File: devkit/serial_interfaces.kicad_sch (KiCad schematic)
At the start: 15 parts, among them J1 Micro_SD_Card, J2 Conn_01x03, J3 Conn_01x04, J4 Conn_01x06, U4 BME280, U5 BH1750, U6 MPU6050

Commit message: chore: actualizo algunas huellas e info en pcb
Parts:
- C6: footprint Capacitor_SMD:CP_Elec_4x5.8 -> Capacitor_SMD:C_0805_2012Metric_Pad1.18x1.45mm_HandSolder
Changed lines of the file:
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@@
 			)
 		)
-		(property "Footprint" "Capacitor_SMD:CP_Elec_4x5.8"
+		(property "Footprint" "Capacitor_SMD:C_0805_2012Metric_Pad1.18x1.45mm_HandSolder"
 			(at 44.1452 140.97 0)
 			(effects

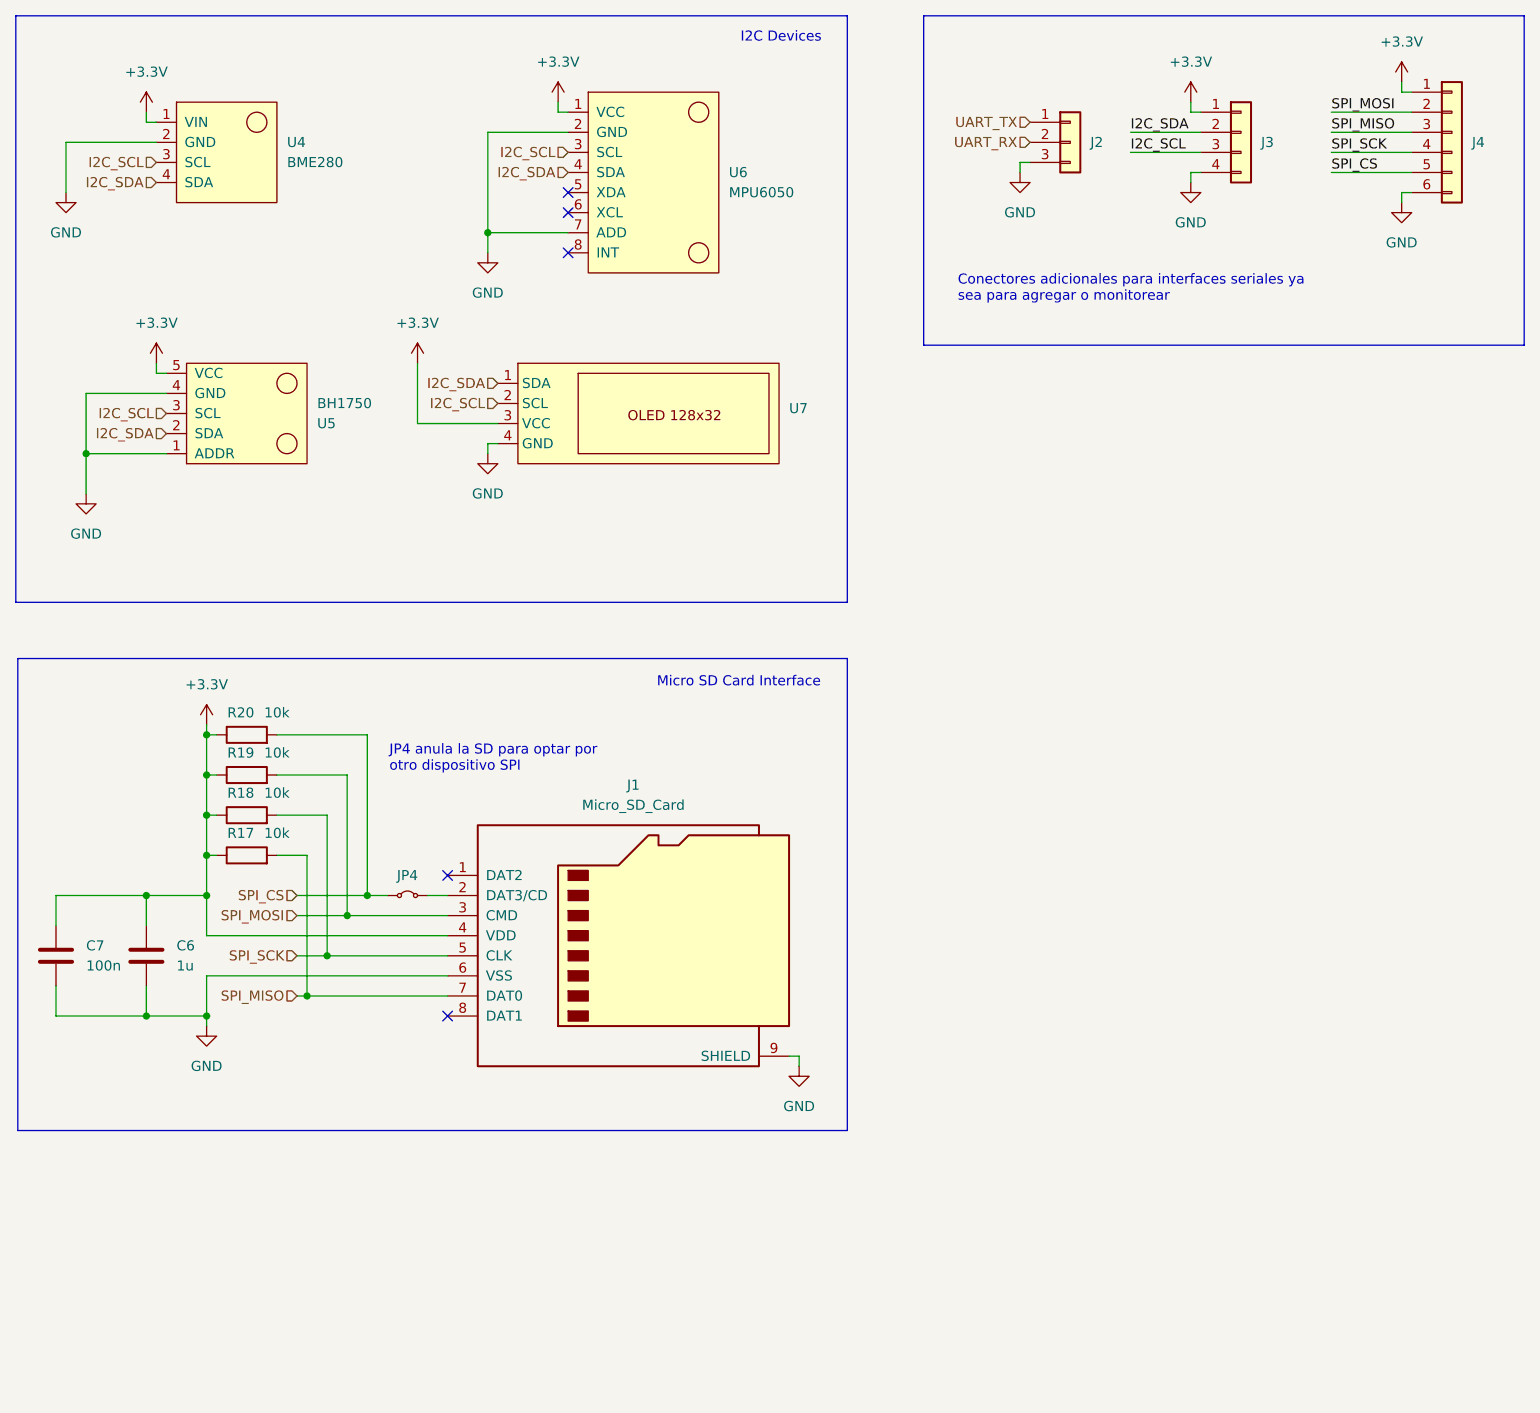
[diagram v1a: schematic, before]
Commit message: feat: adicion de memoria flash
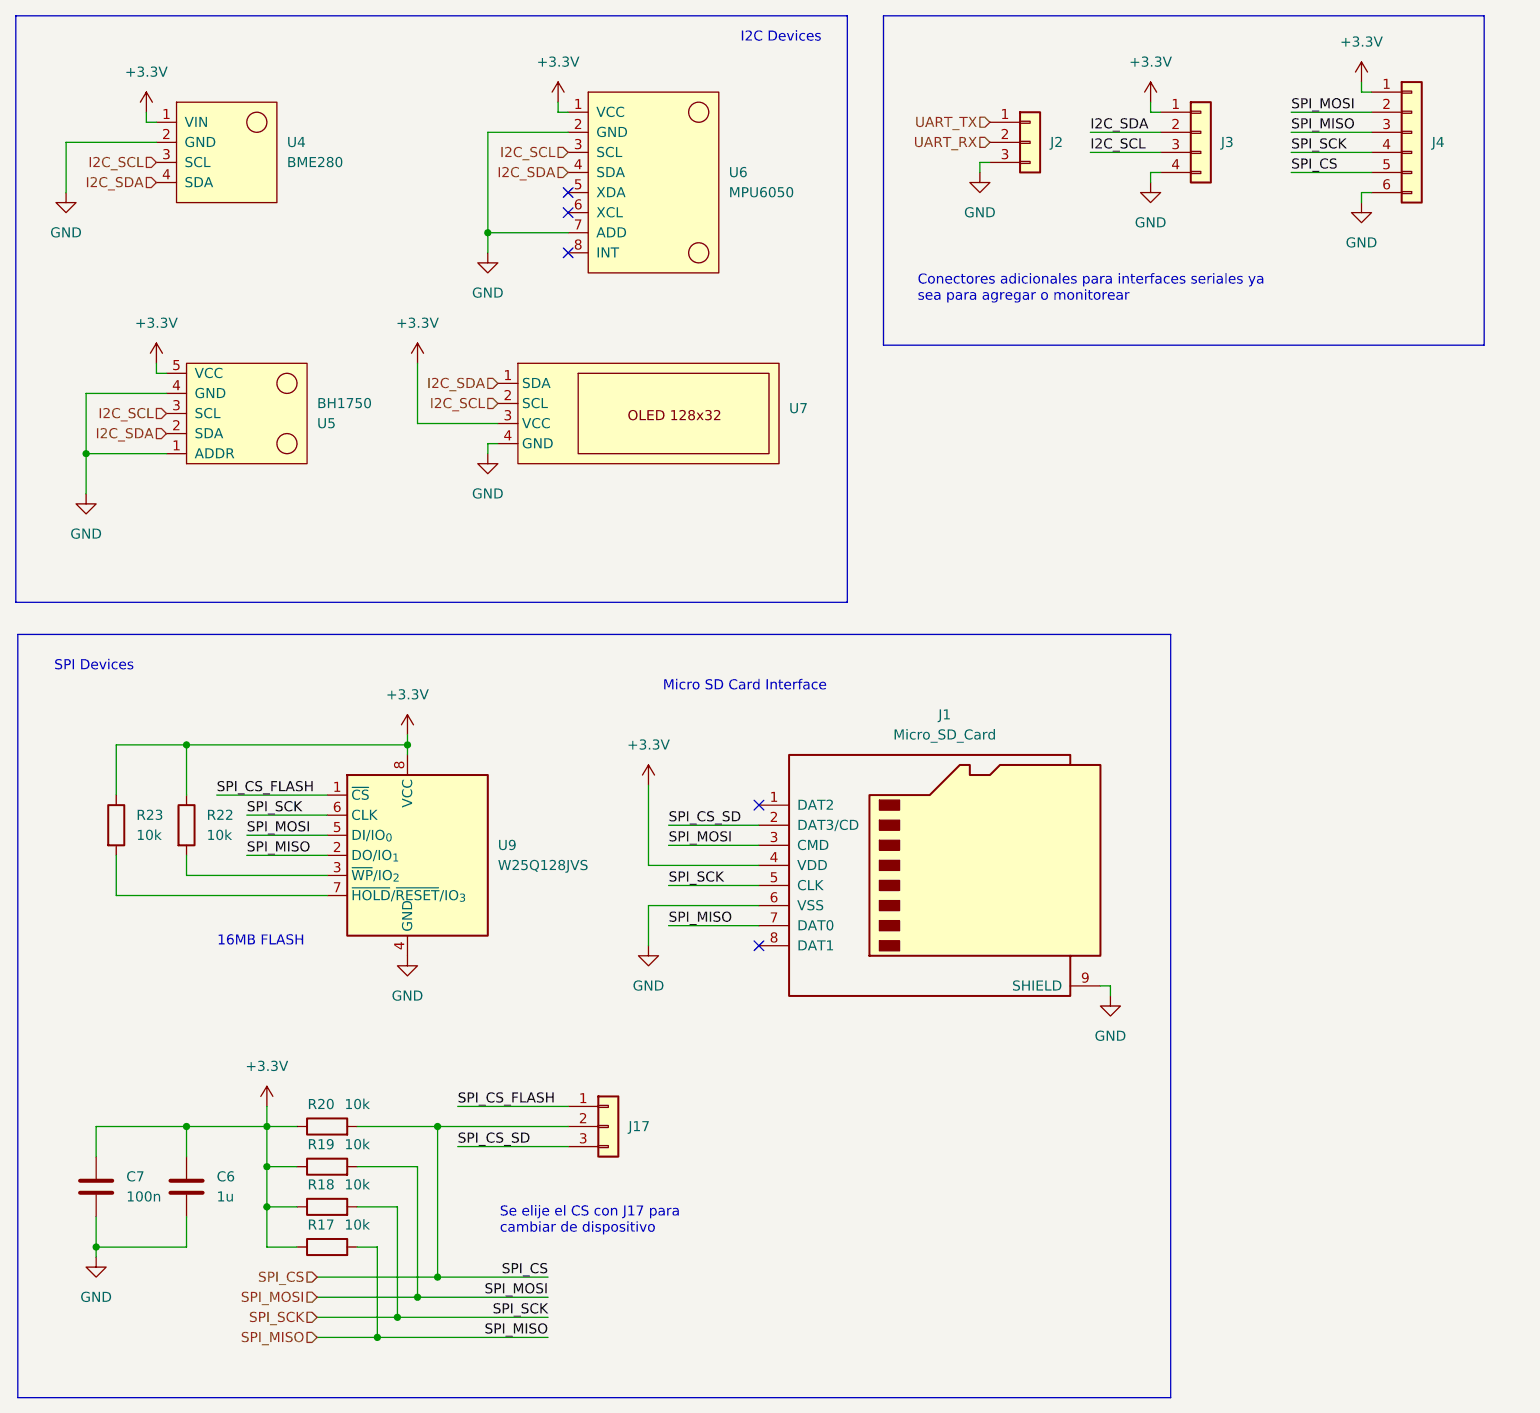
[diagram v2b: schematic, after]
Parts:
- removed JP4: Jumper_2_Small_Bridged, Connector_PinHeader_2.54mm:PinHeader_1x02_P2.54mm_Vertical, symbol Jumper:Jumper_2_Small_Bridged
- added J17: Conn_01x03, Connector_PinHeader_2.54mm:PinHeader_1x03_P2.54mm_Vertical, symbol Connector_Generic:Conn_01x03
- added R22, R23: 10k, Resistor_SMD:R_0805_2012Metric_Pad1.20x1.40mm_HandSolder, symbol Device:R
- added U9: W25Q128JVS, Package_SO:SOIC-8_5.3x5.3mm_P1.27mm, symbol Memory_Flash:W25Q128JVS
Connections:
- net +3.3V: now also R22.1, R23.1, U9.8 (VCC)
- net GND: now also U9.4 (GND)
- net SPI_CS: now also J17.2 (Pin_2)
- net SPI_MISO: now also U9.2 (DO/IO_{1})
- net SPI_MOSI: now also U9.5 (DI/IO_{0})
- net SPI_SCK: now also U9.6 (CLK)
- net SPI_CS_SD: now reaches J1.2 (DAT3/CD)
- net SPI_CS_SD: now also J17.3 (Pin_3)
- new net: R23.2, U9.7 (~{HOLD}/~{RESET}/IO_{3})
- new net: R22.2, U9.3 (~{WP}/IO_{2})
- new net SPI_CS_FLASH: J17.1 (Pin_1), U9.1 (~{CS})
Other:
- note added: "16MB FLASH"
- note added: "SPI Devices"
- note added: "Se elije el CS con J17 para cambiar de dispositivo"
- note removed: "JP4 anula la SD para optar por otro dispositivo SPI"
- moved on the sheet: C6, C7, J1, J2, J3, J4, R17, R18, R19, R20
